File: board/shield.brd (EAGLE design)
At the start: 66 x 57.8 mm, 45 parts, among them IC1 LM75, J1 22-05-7048-04, J2 22-05-7028-02, J4 POWER_JACKPTH, K1 G5L, T1 BC817, U1 LM2596S-5.0

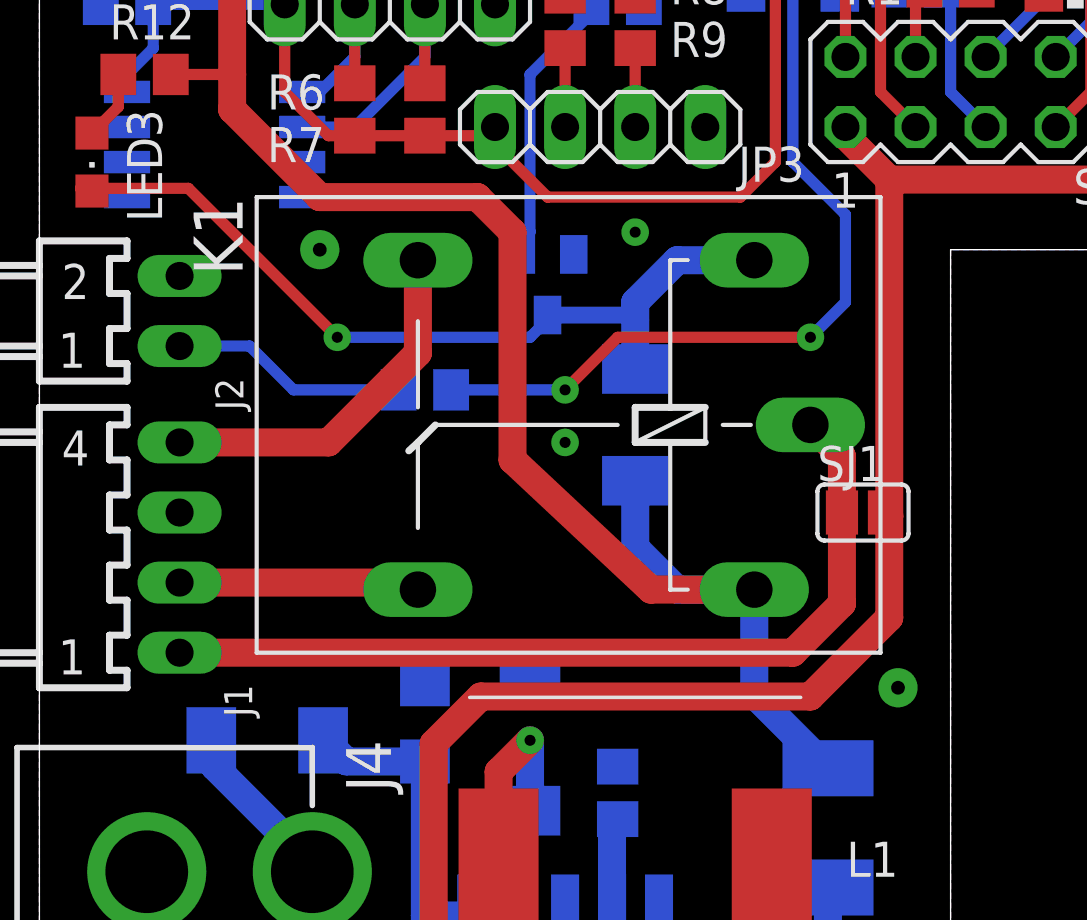
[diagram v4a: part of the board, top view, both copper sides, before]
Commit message: Solder jumper position fix
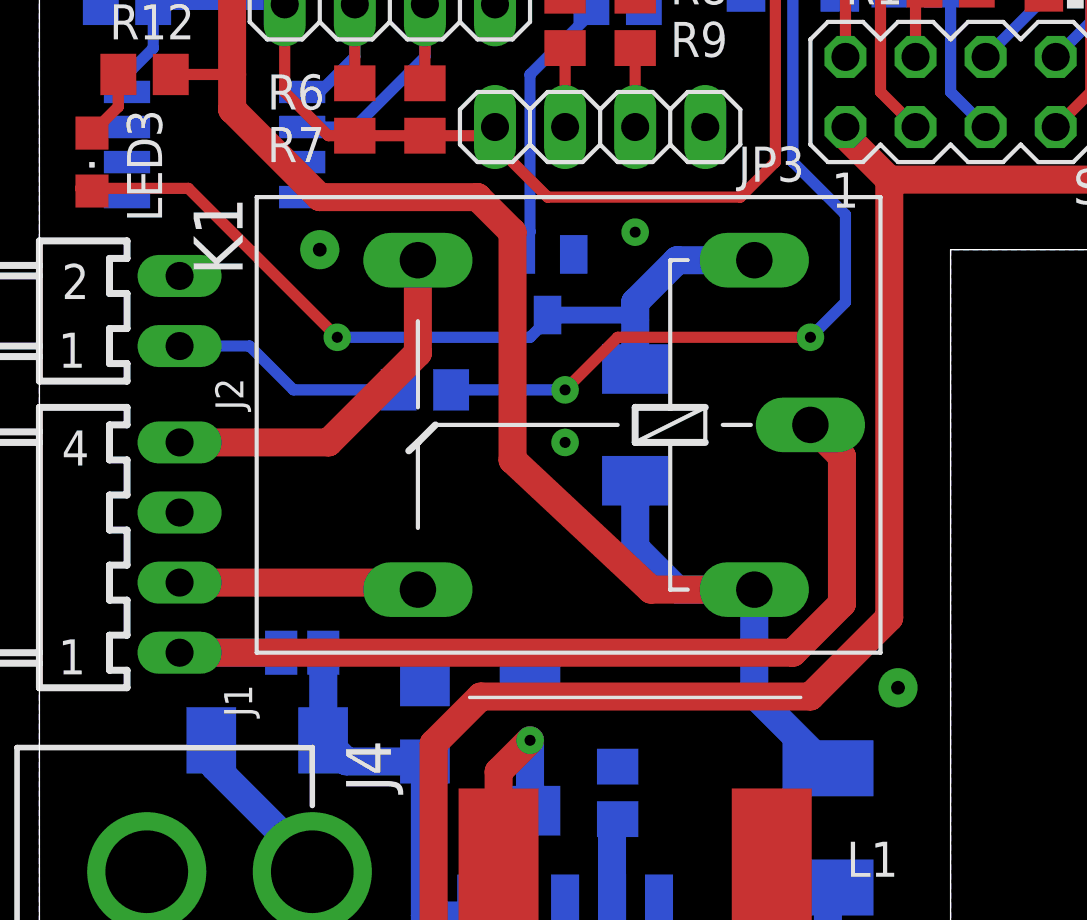
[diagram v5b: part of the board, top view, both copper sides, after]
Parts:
- moved SJ1 20.9 mm to (9.53, 25.4), flipped to the bottom, turned to 180 degrees
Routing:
- net C: track 31.9 -> 35.4 mm
- net +24V: track 94.5 -> 97.5 mm
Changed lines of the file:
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@@
 <layers>
 <layer number="1" name="Top" color="4" fill="1" visible="yes" active="yes"/>
-<layer number="16" name="Bottom" color="1" fill="1" visible="no" active="yes"/>
+<layer number="16" name="Bottom" color="1" fill="1" visible="yes" active="yes"/>
 <layer number="17" name="Pads" color="2" fill="1" visible="yes" active="yes"/>
 <layer number="18" name="Vias" color="2" fill="1" visible="yes" active="yes"/>
 <layer number="19" name="Unrouted" color="6" fill="1" visible="yes" active="yes"/>
 <layer number="20" name="Dimension" color="15" fill="1" visible="yes" active="yes"/>
-<layer number="21" name="tPlace" color="7" fill="1" visible="yes" active="yes"/>
-<layer number="22" name="bPlace" color="7" fill="1" visible="no" active="yes"/>
-<layer number="23" name="tOrigins" color="15" fill="1" visible="yes" active="yes"/>
-<layer number="24" name="bOrigins" color="15" fill="1" visible="no" active="yes"/>
-<layer number="25" name="tNames" color="7" fill="1" visible="yes" active="yes"/>
+<layer number="21" name="tPlace" color="7" fill="1" visible="no" active="yes"/>
+<layer number="22" name="bPlace" color="7" fill="1" visible="yes" active="yes"/>
+<layer number="23" name="tOrigins" color="15" fill="1" visible="no" active="yes"/>
+<layer number="24" name="bOrigins" color="15" fill="1" visible="yes" active="yes"/>
+<layer number="25" name="tNames" color="7" fill="1" visible="no" active="yes"/>
 <layer number="26" name="bNames" color="7" fill="1" visible="no" active="yes"/>
 <layer number="27" name="tValues" color="7" fill="1" visible="no" active="yes"/>
@@
 <layer number="46" name="Milling" color="3" fill="1" visible="no" active="yes"/>
 <layer number="47" name="Measures" color="7" fill="1" visible="no" active="yes"/>
-<layer number="48" name="Document" color="7" fill="1" visible="no" active="yes"/>
+<layer number="48" name="Document" color="7" fill="1" visible="yes" active="yes"/>
 <layer number="49" name="Reference" color="7" fill="1" visible="no" active="yes"/>
 <layer number="50" name="dxf" color="7" fill="1" visible="no" active="no"/>
-<layer number="51" name="tDocu" color="7" fill="1" visible="yes" active="yes"/>
-<layer number="52" name="bDocu" color="7" fill="1" visible="no" active="yes"/>
+<layer number="51" name="tDocu" color="7" fill="1" visible="no" active="yes"/>
+<layer number="52" name="bDocu" color="7" fill="1" visible="yes" active="yes"/>
 <layer number="53" name="tPadExt" color="7" fill="1" visible="no" active="no"/>
 <layer number="54" name="bPadExt" color="1" fill="1" visible="no" active="no"/>
@@
 <attribute name="VALUE" x="2.6401" y="23.2679" size="0.8128" layer="27" ratio="10" rot="R180"/>
 </element>
-<element name="SJ1" library="jumper" package="SJ" value="" x="29.845" y="30.48"/>
+<element name="SJ1" library="jumper" package="SJ" value="" x="9.525" y="25.4" rot="MR180"/>
 </elements>
 <signals>
@@
 <wire x1="46.99" y1="43.815" x2="45.72" y2="42.545" width="1.016" layer="1"/>
 <wire x1="45.72" y1="42.545" x2="30.7975" y2="42.545" width="1.016" layer="1"/>
-<wire x1="30.7975" y1="42.545" x2="30.7975" y2="30.353" width="1.016" layer="1"/>
-<wire x1="30.7975" y1="30.353" x2="30.7975" y2="26.67" width="1.016" layer="1"/>
+<wire x1="30.7975" y1="42.545" x2="30.7975" y2="26.67" width="1.016" layer="1"/>
 <wire x1="30.7975" y1="26.67" x2="27.94" y2="23.8125" width="1.016" layer="1"/>
 <wire x1="15.995" y1="23.8125" x2="27.94" y2="23.8125" width="1.016" layer="1"/>
@@
 <wire x1="10.36" y1="22.225" x2="10.28" y2="22.225" width="0.4064" layer="16"/>
 <contactref element="SJ1" pad="2"/>
-<wire x1="30.607" y1="30.48" x2="30.7975" y2="30.353" width="1.016" layer="1"/>
+<wire x1="10.287" y1="25.4" x2="10.287" y2="22.232" width="1.016" layer="16"/>
+<wire x1="10.287" y1="22.232" x2="10.28" y2="22.225" width="1.016" layer="16"/>
 </signal>
 <signal name="N$4">
@@
 <contactref element="SJ1" pad="1"/>
 <wire x1="5.08" y1="25.4" x2="27.305" y2="25.4" width="1.016" layer="1"/>
-<wire x1="29.083" y1="30.2895" x2="29.083" y2="30.48" width="1.016" layer="1"/>
 <wire x1="27.305" y1="25.4" x2="29.083" y2="27.178" width="1.016" layer="1"/>
-<wire x1="29.083" y1="27.178" x2="29.083" y2="30.48" width="1.016" layer="1"/>
-<wire x1="29.083" y1="30.48" x2="29.083" y2="32.512" width="1.016" layer="1"/>
 <wire x1="29.083" y1="32.512" x2="27.94" y2="33.655" width="1.016" layer="1"/>
+<wire x1="29.083" y1="32.512" x2="29.083" y2="27.178" width="1.016" layer="1"/>
+<wire x1="8.763" y1="25.4" x2="5.08" y2="25.4" width="1.016" layer="16"/>
 </signal>
 </signals>

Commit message: Silkscreen corrected
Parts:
- removed PCB1: RPI3, e14_Rpi3_RevA:RPI3
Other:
- board text added: "2016"
- board text added: "Filip Richter"
- board text added: "Kati v1.2"
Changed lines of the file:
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@@
 <layers>
 <layer number="1" name="Top" color="4" fill="1" visible="yes" active="yes"/>
-<layer number="16" name="Bottom" color="1" fill="1" visible="yes" active="yes"/>
+<layer number="16" name="Bottom" color="1" fill="1" visible="no" active="yes"/>
 <layer number="17" name="Pads" color="2" fill="1" visible="yes" active="yes"/>
 <layer number="18" name="Vias" color="2" fill="1" visible="yes" active="yes"/>
 <layer number="19" name="Unrouted" color="6" fill="1" visible="yes" active="yes"/>
 <layer number="20" name="Dimension" color="15" fill="1" visible="yes" active="yes"/>
-<layer number="21" name="tPlace" color="7" fill="1" visible="no" active="yes"/>
-<layer number="22" name="bPlace" color="7" fill="1" visible="yes" active="yes"/>
-<layer number="23" name="tOrigins" color="15" fill="1" visible="no" active="yes"/>
-<layer number="24" name="bOrigins" color="15" fill="1" visible="yes" active="yes"/>
-<layer number="25" name="tNames" color="7" fill="1" visible="no" active="yes"/>
+<layer number="21" name="tPlace" color="7" fill="1" visible="yes" active="yes"/>
+<layer number="22" name="bPlace" color="7" fill="1" visible="no" active="yes"/>
+<layer number="23" name="tOrigins" color="15" fill="1" visible="yes" active="yes"/>
+<layer number="24" name="bOrigins" color="15" fill="1" visible="no" active="yes"/>
+<layer number="25" name="tNames" color="7" fill="1" visible="yes" active="yes"/>
 <layer number="26" name="bNames" color="7" fill="1" visible="no" active="yes"/>
 <layer number="27" name="tValues" color="7" fill="1" visible="no" active="yes"/>
@@
 <layer number="49" name="Reference" color="7" fill="1" visible="no" active="yes"/>
 <layer number="50" name="dxf" color="7" fill="1" visible="no" active="no"/>
-<layer number="51" name="tDocu" color="7" fill="1" visible="no" active="yes"/>
-<layer number="52" name="bDocu" color="7" fill="1" visible="yes" active="yes"/>
+<layer number="51" name="tDocu" color="7" fill="1" visible="yes" active="yes"/>
+<layer number="52" name="bDocu" color="7" fill="1" visible="no" active="yes"/>
 <layer number="53" name="tPadExt" color="7" fill="1" visible="no" active="no"/>
 <layer number="54" name="bPadExt" color="1" fill="1" visible="no" active="no"/>
@@
 <wire x1="66.04" y1="57.785" x2="0" y2="57.785" width="0" layer="20"/>
 <wire x1="0" y1="57.785" x2="0" y2="0" width="0" layer="20"/>
+<text x="59.69" y="41.91" size="1.778" layer="25">Kati
+v1.2</text>
+<text x="29.845" y="11.1125" size="1.778" layer="25" rot="R90">Filip Richter</text>
+<text x="32.0675" y="14.9225" size="1.778" layer="25" rot="R90">2016</text>
 </plain>
 <attributes>
@@
 <attribute name="SUPPLIER" value="Wuerth Elektronik" x="21.59" y="17.78" size="1.778" layer="27" display="off"/>
 <attribute name="OC_NEWARK" value="08P2779" x="21.59" y="17.78" size="1.778" layer="27" display="off"/>
-<attribute name="NAME" x="29.25" y="17.28" size="1.27" layer="25"/>
+<attribute name="NAME" x="13.375" y="11.565" size="1.27" layer="25"/>
 <attribute name="VALUE" x="15.78" y="25.13" size="1.27" layer="27"/>
 </element>
@@
 <attribute name="VALUE" x="13.208" y="19.7358" size="2.0828" layer="28" ratio="10" rot="SMR180"/>
 </element>
-<element name="PCB1" library="e14_Rpi3_RevA" package="RPI3" value="RPI3" x="122.36" y="-1.375" rot="R90"/>
 <element name="J2" library="con-molex" package="7395-02" value="22-05-7028-02" x="5.08" y="37.7825" smashed="yes" rot="R270">
 <attribute name="OC_FARNELL" value="9731601" x="5.08" y="37.7825" size="1.778" layer="27" rot="R270" display="off"/>
@@
 <attribute name="OC_NEWARK" value="unknown" x="34.29" y="45.72" size="1.778" layer="27" display="off"/>
 <attribute name="MF" value="" x="34.29" y="45.72" size="1.778" layer="27" display="off"/>
-<attribute name="NAME" x="37.465" y="41.656" size="1.27" layer="25" ratio="10"/>
+<attribute name="NAME" x="40.9575" y="46.736" size="1.27" layer="25" ratio="10"/>
 <attribute name="VALUE" x="34.29" y="41.529" size="1.27" layer="27" ratio="10"/>
 </element>
@@
 <attribute name="OC_NEWARK" value="unknown" x="52.07" y="45.72" size="1.778" layer="27" display="off"/>
 <attribute name="MF" value="" x="52.07" y="45.72" size="1.778" layer="27" display="off"/>
-<attribute name="NAME" x="55.245" y="41.656" size="1.27" layer="25" ratio="10"/>
+<attribute name="NAME" x="58.7375" y="46.736" size="1.27" layer="25" ratio="10"/>
 <attribute name="VALUE" x="52.07" y="41.529" size="1.27" layer="27" ratio="10"/>
 </element>
@@
 </board>
 </drawing>
+<compatibility>
+<note version="6.3" minversion="6.2.2" severity="warning">
+Since Version 6.2.2 text objects can contain more than one line,
+which will not be processed correctly with this version.
+</note>
+</compatibility>
 </eagle>
